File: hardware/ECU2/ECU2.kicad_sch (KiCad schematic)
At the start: 31 parts, among them J1 Conn_fuel, J2 Conn_speed, J3 Conn_fuel_gauge, J4 Conn_RPM, U1 step down (buck), U2 ESP32-WROOM-32

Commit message: add images to README
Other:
- note added: "DECOUPLING"
- moved on the sheet: C1, C10, C11, C12, C13, C14, C15, C16, C17, C18, C2, C3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

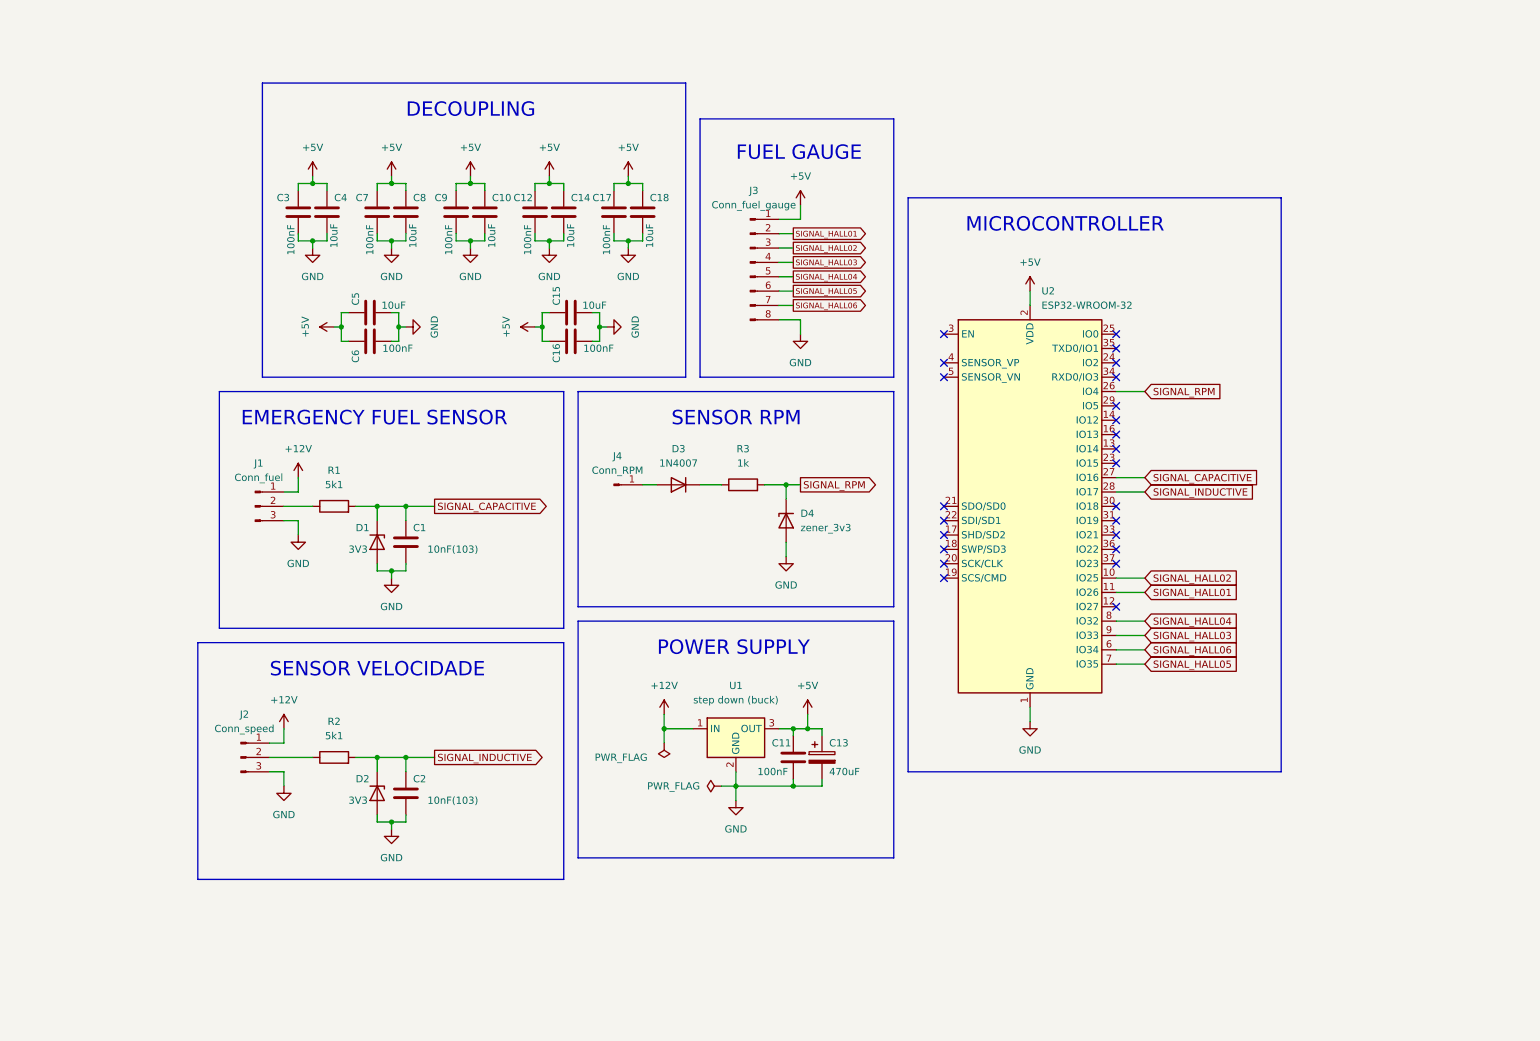
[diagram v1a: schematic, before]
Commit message: add alive LED
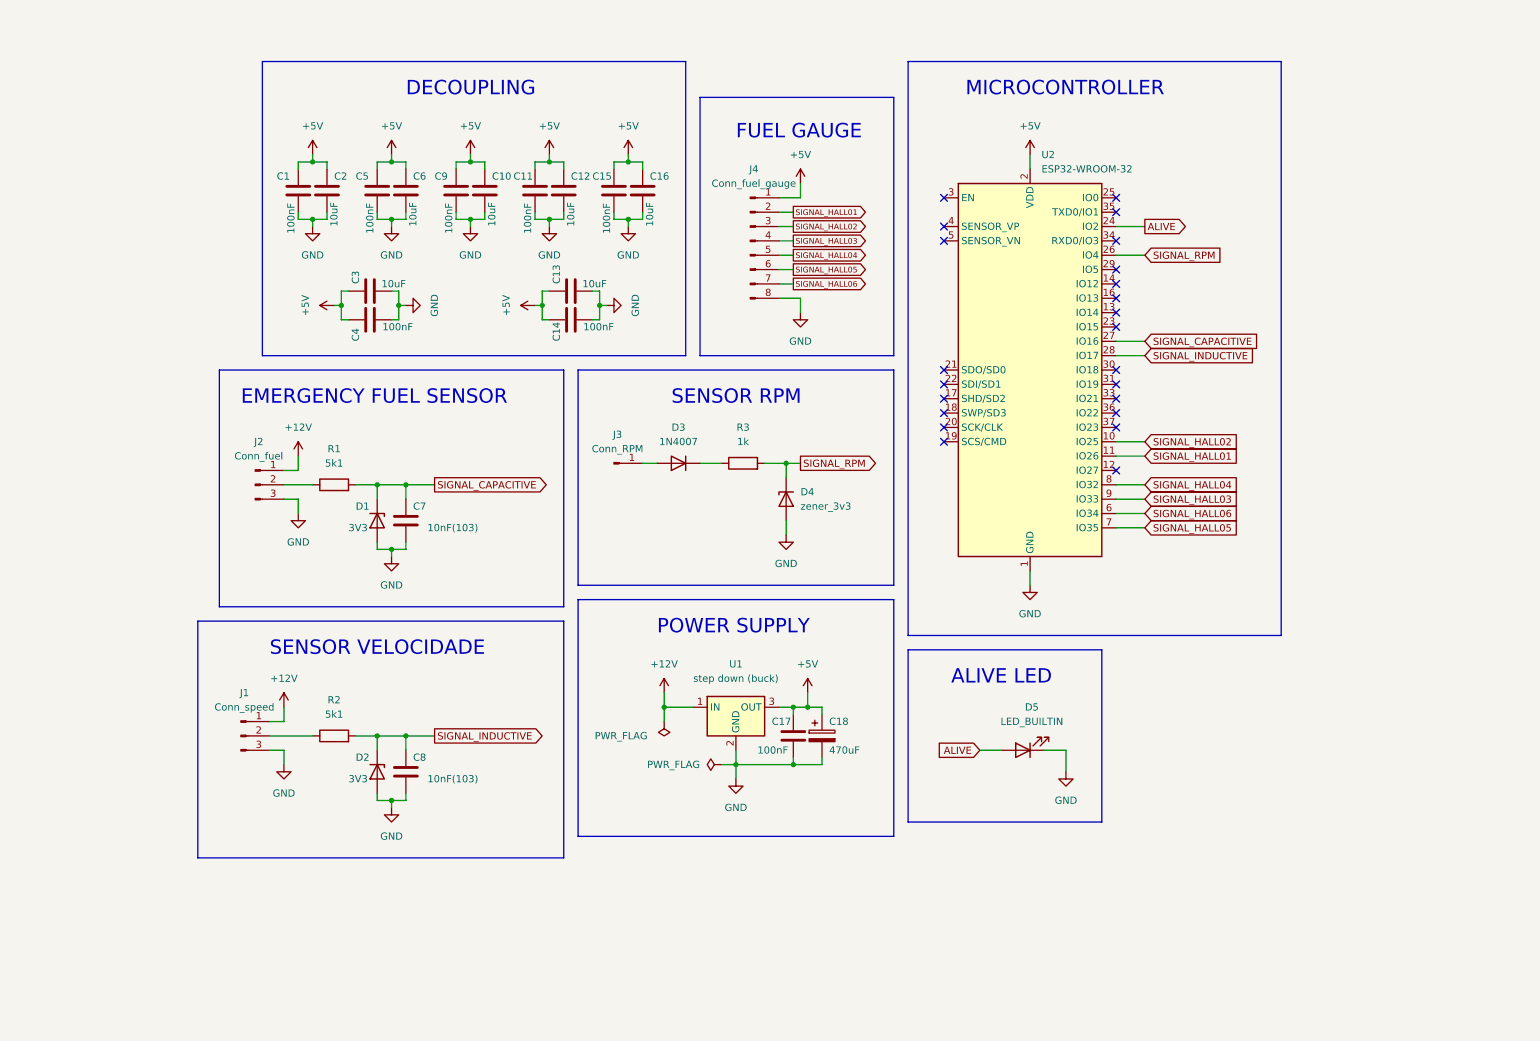
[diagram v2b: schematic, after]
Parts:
- added D5: LED_BUILTIN, symbol Device:LED
- renumbered C3 to C1, C12 to C11, C14 to C12, C15 to C13, C16 to C14, C17 to C15, C18 to C16, C11 to C17, C13 to C18, C4 to C2, C5 to C3, C6 to C4, C7 to C5, C8 to C6, C1 to C7, C2 to C8, J2 to J1, J1 to J2, J4 to J3, J3 to J4
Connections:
- net GND: now also D5.1 (K)
- net ALIVE: now reaches U2.24 (IO2)
- net ALIVE: now also D5.2 (A)
- no-connect marks 24 -> 23
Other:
- note added: "ALIVE LED"
- moved on the sheet: C1, C10, C11, C12, C13, C14, C15, C16, C17, C18, C2, C3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

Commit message: change hall pinout
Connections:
- net SIGNAL_HALL01: now also U2.13 (IO14); no longer U2.11 (IO26)
- net SIGNAL_HALL02: now also U2.12 (IO27); no longer U2.10 (IO25)
- net SIGNAL_HALL03: now also U2.11 (IO26); no longer U2.9 (IO33)
- net SIGNAL_HALL04: now also U2.10 (IO25); no longer U2.8 (IO32)
- net SIGNAL_HALL05: now also U2.9 (IO33); no longer U2.7 (IO35)
- net SIGNAL_HALL06: now also U2.8 (IO32); no longer U2.6 (IO34)
